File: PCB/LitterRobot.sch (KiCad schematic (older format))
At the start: 5 parts, among them J1 DF11C-4DP-2V(57), J2 DF11C-6DP-2V(57), J3 DF11C-8DP-2V(57), J4 DF11C-6DP-2V(57)

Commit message: Initial commit of the Quartus project
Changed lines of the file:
@@
 F0 "Motor driver" 50
 F1 "MotorDriver.sch" 50
-F2 "Motor_PWM_P" I L 9000 4600 50
-F3 "Motor_PWM_N" I L 9000 4700 50
+F2 "Motor_PWM_1" I L 9000 4600 50
+F3 "Motor_PWM_2" I L 9000 4700 50
 F4 "Motor_P" O R 10000 4800 50
 F5 "Motor_N" O R 10000 4900 50
@@
 F0 "FPGA" 50
 F1 "FPGA.sch" 50
-F2 "Motor_PWM_P" O R 7500 4600 50
-F3 "Motor_PWM_N" O R 7500 4700 50
+F2 "Motor_PWM_1" O R 7500 4600 50
+F3 "Motor_PWM_2" O R 7500 4700 50
 F4 "Cycle_button" I L 6000 1350 50
 F5 "Empty_button" I L 6000 1450 50

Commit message: Add the FPGA symbol
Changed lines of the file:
@@
 $Descr A4 11693 8268
 encoding utf-8
-Sheet 1 17
+Sheet 1 19
 Title "Litter Robot 3 - Main board"
 Date "2021-02-27"
@@
 Wire Wire Line
 	2600 4750 3500 4750
+Wire Wire Line
+	7500 1550 9000 1550
+Wire Wire Line
+	9000 1650 7500 1650
+Wire Wire Line
+	7500 1750 9000 1750
+Wire Wire Line
+	7500 1900 9000 1900
+Wire Wire Line
+	7500 2000 9000 2000
+Wire Wire Line
+	9000 2100 7500 2100
+Wire Wire Line
+	7500 2250 9000 2250
+Wire Wire Line
+	9000 2350 7500 2350
+Wire Wire Line
+	7500 2450 9000 2450
+Wire Wire Line
+	7500 2600 9000 2600
+Wire Wire Line
+	7500 2700 9000 2700
+Wire Wire Line
+	9000 2800 7500 2800
+Wire Wire Line
+	7500 2950 9000 2950
+Wire Wire Line
+	9000 3050 7500 3050
+Wire Wire Line
+	7500 3150 9000 3150
+Wire Wire Line
+	7500 3300 9000 3300
+Wire Wire Line
+	7500 3400 9000 3400
+Wire Wire Line
+	9000 3500 7500 3500
+Wire Wire Line
+	7500 3650 9000 3650
+Wire Wire Line
+	9000 3750 7500 3750
+Wire Wire Line
+	7500 3850 9000 3850
+Wire Wire Line
+	7500 4600 9000 4600
+Wire Wire Line
+	9000 4700 7500 4700
+$Sheet
+S 4000 1000 1000 500
+U 603F1DCE
+F0 "Power supply" 50
+F1 "PowerSupply.sch" 50
+F2 "Power_good" O R 5000 1100 50
+$EndSheet
+Wire Wire Line
+	10000 1200 10750 1200
+Text Label 10750 1100 2    50   ~ 0
+Power_button
+Text Label 10750 1200 2    50   ~ 0
+Cycle_button
+Wire Wire Line
+	10000 1100 10750 1100
+Wire Wire Line
+	10000 1400 10750 1400
+Text Label 10750 1300 2    50   ~ 0
+Empty_button
+Text Label 10750 1400 2    50   ~ 0
+Reset_button
+Wire Wire Line
+	10000 1300 10750 1300
+Wire Wire Line
+	6000 1350 5250 1350
+Text Label 5250 1250 0    50   ~ 0
+Power_button
+Text Label 5250 1350 0    50   ~ 0
+Cycle_button
+Wire Wire Line
+	6000 1250 5250 1250
+Wire Wire Line
+	6000 1550 5250 1550
+Text Label 5250 1450 0    50   ~ 0
+Empty_button
+Text Label 5250 1550 0    50   ~ 0
+Reset_button
+Wire Wire Line
+	6000 1450 5250 1450
+Text Label 8250 1100 2    50   ~ 0
+Dome_LED
+Wire Wire Line
+	7500 1100 8250 1100
+Wire Wire Line
+	1000 4750 2000 4750
+Text Label 1000 4750 0    50   ~ 0
+Cat_sensor_P
+Wire Wire Line
+	5000 1100 6000 1100
+Wire Wire Line
+	2500 1550 3500 1550
+Wire Wire Line
+	1000 1650 2000 1650
+Text Label 1000 1650 0    50   ~ 0
+TODO_2
+Text Label 3500 1550 2    50   ~ 0
+TODO_1
+$Comp
+L Device:Polyfuse F1
+U 1 1 6061774B
+P 1250 2750
+F 0 "F1" H 1338 2796 50  0000 L CNN
+F 1 "Polyfuse" H 1338 2705 50  0000 L CNN
+F 2 "LitterRobot:Bel_Fuse_0ZCG" H 1300 2550 50  0001 L CNN
+F 3 "https://www.belfuse.com/resources/datasheets/circuitprotection/ds-cp-0zcg-series.pdf" H 1250 2750 50  0001 C CNN
+F 4 "0ZCG0110BF2B" H 1250 2750 50  0001 C CNN "Part_number"
+	1    1250 2750
+	1    0    0    -1
+$EndComp
+$Comp
+L power:+15V #PWR01
+U 1 1 6046C18F
+P 1250 2500
+F 0 "#PWR01" H 1250 2350 50  0001 C CNN
+F 1 "+15V" H 1265 2673 50  0000 C CNN
+F 2 "" H 1250 2500 50  0001 C CNN
+F 3 "" H 1250 2500 50  0001 C CNN
+	1    1250 2500
+	1    0    0    -1
+$EndComp
+Wire Wire Line
+	1250 2500 1250 2600
+Wire Wire Line
+	1250 2900 1250 3050
+Wire Wire Line
+	1250 3050 2000 3050
+Text Notes 4000 7300 0    98   ~ 0
+TODO:\n- Reverse polarity protection diode\n- Hall sensors (2 V diode for the supply + 2 × MOS level shifter)\n- Cat sensor\n- Tray full sensor\n- Pinch sensor\n- Dome LED\n- Power good → FPGA reset\n\nTODO later:\n- Bluetooth (MDBT40?)
+Text Label 1000 4850 0    50   ~ 0
+Dome_LED_P
+Text Label 3500 4750 2    50   ~ 0
+Cat_sensor_N
+Text Label 3500 4850 2    50   ~ 0
+Dome_LED_N
+$Comp
+L power:+15V #PWR03
+U 1 1 60622B0D
+P 1650 5950
+F 0 "#PWR03" H 1650 5800 50  0001 C CNN
+F 1 "+15V" H 1665 6123 50  0000 C CNN
+F 2 "" H 1650 5950 50  0001 C CNN
+F 3 "" H 1650 5950 50  0001 C CNN
+	1    1650 5950
+	1    0    0    -1
+$EndComp
+$Sheet
+S 4000 2000 1000 500
+U 60624089
+F0 "Light sensor" 50
+F1 "LightSensor.sch" 50
+F2 "Light_sensor_SDA" B R 5000 2100 50
+F3 "Light_sensor_SCL" I R 5000 2200 50
+F4 "Light_sensor_INT" O R 5000 2300 50
+$EndSheet
+Wire Wire Line
+	5000 2100 6000 2100
+Wire Wire Line
+	6000 2200 5000 2200
+Wire Wire Line
+	5000 2300 6000 2300
 $Sheet
 S 6000 1000 1500 4000
 U 603F1F4D
 F0 "FPGA" 50
-F1 "FPGA.sch" 50
+F1 "Fpga.sch" 50
 F2 "Motor_PWM_1" O R 7500 4600 50
 F3 "Motor_PWM_2" O R 7500 4700 50
@@
 F33 "Light_sensor_INT" I L 6000 2300 50
 $EndSheet
-Wire Wire Line
-	7500 1550 9000 1550
-Wire Wire Line
-	9000 1650 7500 1650
-Wire Wire Line
-	7500 1750 9000 1750
-Wire Wire Line
-	7500 1900 9000 1900
-Wire Wire Line
-	7500 2000 9000 2000
-Wire Wire Line
-	9000 2100 7500 2100
-Wire Wire Line
-	7500 2250 9000 2250
-Wire Wire Line
-	9000 2350 7500 2350
-Wire Wire Line
-	7500 2450 9000 2450
-Wire Wire Line
-	7500 2600 9000 2600
-Wire Wire Line
-	7500 2700 9000 2700
-Wire Wire Line
-	9000 2800 7500 2800
-Wire Wire Line
-	7500 2950 9000 2950
-Wire Wire Line
-	9000 3050 7500 3050
-Wire Wire Line
-	7500 3150 9000 3150
-Wire Wire Line
-	7500 3300 9000 3300
-Wire Wire Line
-	7500 3400 9000 3400
-Wire Wire Line
-	9000 3500 7500 3500
-Wire Wire Line
-	7500 3650 9000 3650
-Wire Wire Line
-	9000 3750 7500 3750
-Wire Wire Line
-	7500 3850 9000 3850
-Wire Wire Line
-	7500 4600 9000 4600
-Wire Wire Line
-	9000 4700 7500 4700
-$Sheet
-S 4000 1000 1000 500
-U 603F1DCE
-F0 "Power supply" 50
-F1 "PowerSupply.sch" 50
-F2 "Power_good" O R 5000 1100 50
-$EndSheet
-Wire Wire Line
-	10000 1200 10750 1200
-Text Label 10750 1100 2    50   ~ 0
-Power_button
-Text Label 10750 1200 2    50   ~ 0
-Cycle_button
-Wire Wire Line
-	10000 1100 10750 1100
-Wire Wire Line
-	10000 1400 10750 1400
-Text Label 10750 1300 2    50   ~ 0
-Empty_button
-Text Label 10750 1400 2    50   ~ 0
-Reset_button
-Wire Wire Line
-	10000 1300 10750 1300
-Wire Wire Line
-	6000 1350 5250 1350
-Text Label 5250 1250 0    50   ~ 0
-Power_button
-Text Label 5250 1350 0    50   ~ 0
-Cycle_button
-Wire Wire Line
-	6000 1250 5250 1250
-Wire Wire Line
-	6000 1550 5250 1550
-Text Label 5250 1450 0    50   ~ 0
-Empty_button
-Text Label 5250 1550 0    50   ~ 0
-Reset_button
-Wire Wire Line
-	6000 1450 5250 1450
-Text Label 8250 1100 2    50   ~ 0
-Dome_LED
-Wire Wire Line
-	7500 1100 8250 1100
-Wire Wire Line
-	1000 4750 2000 4750
-Text Label 1000 4750 0    50   ~ 0
-Cat_sensor_P
-Wire Wire Line
-	5000 1100 6000 1100
-Wire Wire Line
-	2500 1550 3500 1550
-Wire Wire Line
-	1000 1650 2000 1650
-Text Label 1000 1650 0    50   ~ 0
-TODO_2
-Text Label 3500 1550 2    50   ~ 0
-TODO_1
-$Comp
-L Device:Polyfuse F1
-U 1 1 6061774B
-P 1250 2750
-F 0 "F1" H 1338 2796 50  0000 L CNN
-F 1 "Polyfuse" H 1338 2705 50  0000 L CNN
-F 2 "LitterRobot:Bel_Fuse_0ZCG" H 1300 2550 50  0001 L CNN
-F 3 "https://www.belfuse.com/resources/datasheets/circuitprotection/ds-cp-0zcg-series.pdf" H 1250 2750 50  0001 C CNN
-F 4 "0ZCG0110BF2B" H 1250 2750 50  0001 C CNN "Part_number"
-	1    1250 2750
-	1    0    0    -1
-$EndComp
-$Comp
-L power:+15V #PWR01
-U 1 1 6046C18F
-P 1250 2500
-F 0 "#PWR01" H 1250 2350 50  0001 C CNN
-F 1 "+15V" H 1265 2673 50  0000 C CNN
-F 2 "" H 1250 2500 50  0001 C CNN
-F 3 "" H 1250 2500 50  0001 C CNN
-	1    1250 2500
-	1    0    0    -1
-$EndComp
-Wire Wire Line
-	1250 2500 1250 2600
-Wire Wire Line
-	1250 2900 1250 3050
-Wire Wire Line
-	1250 3050 2000 3050
-Text Notes 4000 7300 0    98   ~ 0
-TODO:\n- Reverse polarity protection diode\n- Hall sensors (2 V diode for the supply + 2 × MOS level shifter)\n- Cat sensor\n- Tray full sensor\n- Pinch sensor\n- Dome LED\n- Power good → FPGA reset\n\nTODO later:\n- Bluetooth (MDBT40?)
-Text Label 1000 4850 0    50   ~ 0
-Dome_LED_P
-Text Label 3500 4750 2    50   ~ 0
-Cat_sensor_N
-Text Label 3500 4850 2    50   ~ 0
-Dome_LED_N
-$Comp
-L power:+15V #PWR03
-U 1 1 60622B0D
-P 1650 5950
-F 0 "#PWR03" H 1650 5800 50  0001 C CNN
-F 1 "+15V" H 1665 6123 50  0000 C CNN
-F 2 "" H 1650 5950 50  0001 C CNN
-F 3 "" H 1650 5950 50  0001 C CNN
-	1    1650 5950
-	1    0    0    -1
-$EndComp
-$Sheet
-S 4000 2000 1000 500
-U 60624089
-F0 "Light sensor" 50
-F1 "LightSensor.sch" 50
-F2 "Light_sensor_SDA" B R 5000 2100 50
-F3 "Light_sensor_SCL" I R 5000 2200 50
-F4 "Light_sensor_INT" O R 5000 2300 50
-$EndSheet
-Wire Wire Line
-	5000 2100 6000 2100
-Wire Wire Line
-	6000 2200 5000 2200
-Wire Wire Line
-	5000 2300 6000 2300
 $EndSCHEMATC

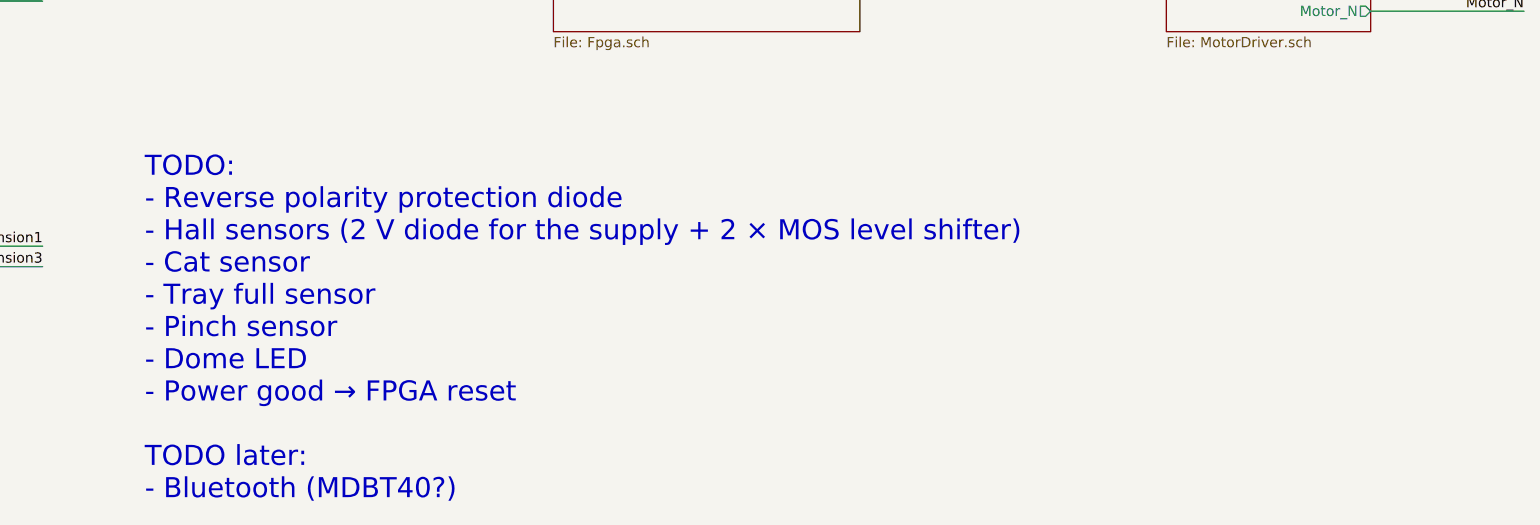
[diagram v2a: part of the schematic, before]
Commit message: Connect the FPGA configuration signals
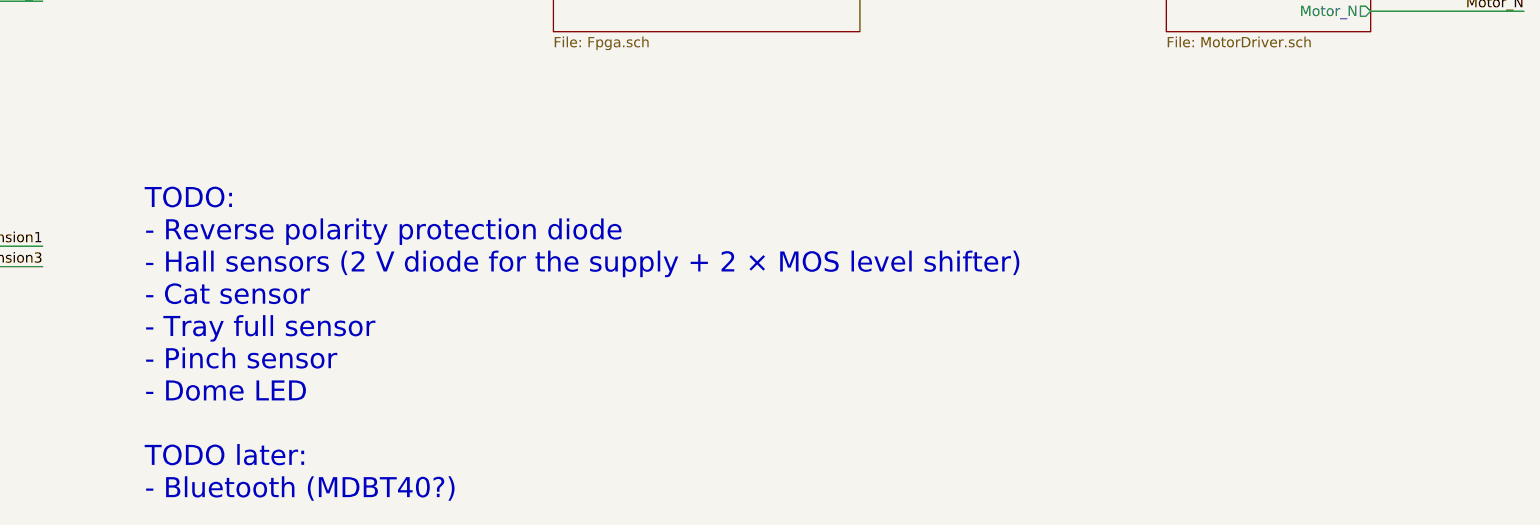
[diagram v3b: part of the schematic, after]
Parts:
- J1: Part_Number DF11C-4DP-2V(57) -> (none); Part_number (none) -> DF11C-4DP-2V(57)
- J2, J4: Part_Number DF11C-6DP-2V(57) -> (none); Part_number (none) -> DF11C-6DP-2V(57)
- J3: Part_Number DF11C-8DP-2V(57) -> (none); Part_number (none) -> DF11C-8DP-2V(57)
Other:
- note added: "TODO:\n- Reverse polarity protection diode\n- Hall sensors (2 V diode for the supply + 2 × MOS level shifter)\n- Cat sensor\n- Tray full sensor\n- Pinch sensor\n- Dome LED\n\nTODO later:\n- Bluetooth (MDBT40?)"
- note removed: "TODO:\n- Reverse polarity protection diode\n- Hall sensors (2 V diode for the supply + 2 × MOS level shifter)\n- Cat sensor\n- Tray full sensor\n- Pinch sensor\n- Dome LED\n- Power good → FPGA reset\n\nTODO later:\n- Bluetooth (MDBT40?)"
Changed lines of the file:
@@
 F 2 "LitterRobot:Hirose_DF11C-6DP-2V(57)" H 2200 3150 50  0001 C CNN
 F 3 "https://www.hirose.com/en/product/document?clcode=CL0543-0683-4-57&productname=DF11C-6DP-2V(57)&series=DF11&documenttype=2DDrawing&lang=en&documentid=0000926113" H 2200 3150 50  0001 C CNN
-F 4 "DF11C-6DP-2V(57)" H 2200 3150 50  0001 C CNN "Part_Number"
+F 4 "" H 2200 3150 50  0001 C CNN "Part_Number"
+F 5 "DF11C-6DP-2V(57)" H 2200 3150 50  0001 C CNN "Part_number"
 	1    2200 3150
 	1    0    0    -1
@@
 F 2 "LitterRobot:Hirose_DF11C-4DP-2V(57)" H 2200 1550 50  0001 C CNN
 F 3 "https://www.hirose.com/en/product/document?clcode=CL0543-0682-1-57&productname=DF11C-4DP-2V(57)&series=DF11&documenttype=2DDrawing&lang=en&documentid=0000926110" H 2200 1550 50  0001 C CNN
-F 4 "DF11C-4DP-2V(57)" H 2200 1550 50  0001 C CNN "Part_Number"
+F 4 "" H 2200 1550 50  0001 C CNN "Part_Number"
+F 5 "DF11C-4DP-2V(57)" H 2200 1550 50  0001 C CNN "Part_number"
 	1    2200 1550
 	1    0    0    -1
@@
 F 2 "LitterRobot:Hirose_DF11C-6DP-2V(57)" H 2200 6150 50  0001 C CNN
 F 3 "https://www.hirose.com/en/product/document?clcode=CL0543-0683-4-57&productname=DF11C-6DP-2V(57)&series=DF11&documenttype=2DDrawing&lang=en&documentid=0000926113" H 2200 6150 50  0001 C CNN
-F 4 "DF11C-6DP-2V(57)" H 2200 6150 50  0001 C CNN "Part_Number"
+F 4 "" H 2200 6150 50  0001 C CNN "Part_Number"
+F 5 "DF11C-6DP-2V(57)" H 2200 6150 50  0001 C CNN "Part_number"
 	1    2200 6150
 	1    0    0    -1
@@
 F 2 "LitterRobot:Hirose_DF11C-8DP-2V(57)" H 2200 4650 50  0001 C CNN
 F 3 "https://www.hirose.com/en/product/document?clcode=CL0543-0684-7-57&productname=DF11C-8DP-2V(57)&series=DF11&documenttype=2DDrawing&lang=en&documentid=0000999153" H 2200 4650 50  0001 C CNN
-F 4 "DF11C-8DP-2V(57)" H 2200 4650 50  0001 C CNN "Part_Number"
+F 4 "" H 2200 4650 50  0001 C CNN "Part_Number"
+F 5 "DF11C-8DP-2V(57)" H 2200 4650 50  0001 C CNN "Part_number"
 	1    2200 4650
 	1    0    0    -1
@@
 	1250 3050 2000 3050
 Text Notes 4000 7300 0    98   ~ 0
-TODO:\n- Reverse polarity protection diode\n- Hall sensors (2 V diode for the supply + 2 × MOS level shifter)\n- Cat sensor\n- Tray full sensor\n- Pinch sensor\n- Dome LED\n- Power good → FPGA reset\n\nTODO later:\n- Bluetooth (MDBT40?)
+TODO:\n- Reverse polarity protection diode\n- Hall sensors (2 V diode for the supply + 2 × MOS level shifter)\n- Cat sensor\n- Tray full sensor\n- Pinch sensor\n- Dome LED\n\nTODO later:\n- Bluetooth (MDBT40?)
 Text Label 1000 4850 0    50   ~ 0
 Dome_LED_P
